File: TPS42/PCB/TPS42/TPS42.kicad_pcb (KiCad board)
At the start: 2 copper layers, 138.1 x 89.7 mm, 67 parts, among them J11 Conn_01x06, J3 TP Sensor Module, J4 TP Module, J5 Conn_01x02, J7 TrackPoint, J8 Battery, J9 TP Sensor Module, SW1 SW_DPST_x2, SW2 Reset, SW3 Reset, U1 ProMicro, U11 Hole, U12 Hole, U14 ProMicro, U4 Hole, U5 Hole, U7 Hole, U8 Hole, U9 Hole

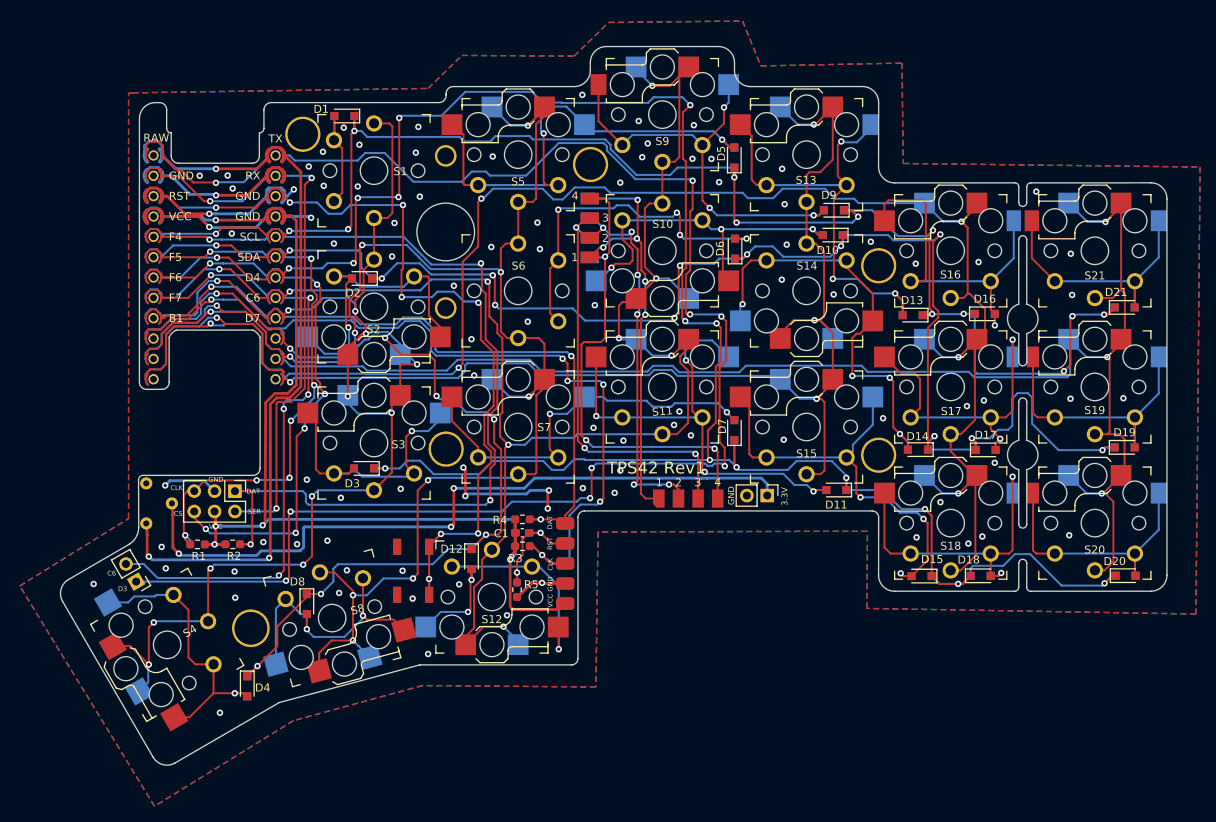
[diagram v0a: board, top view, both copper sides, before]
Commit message: TPS42: clean up the pcb a bit, get rid of the oled/lcd shields
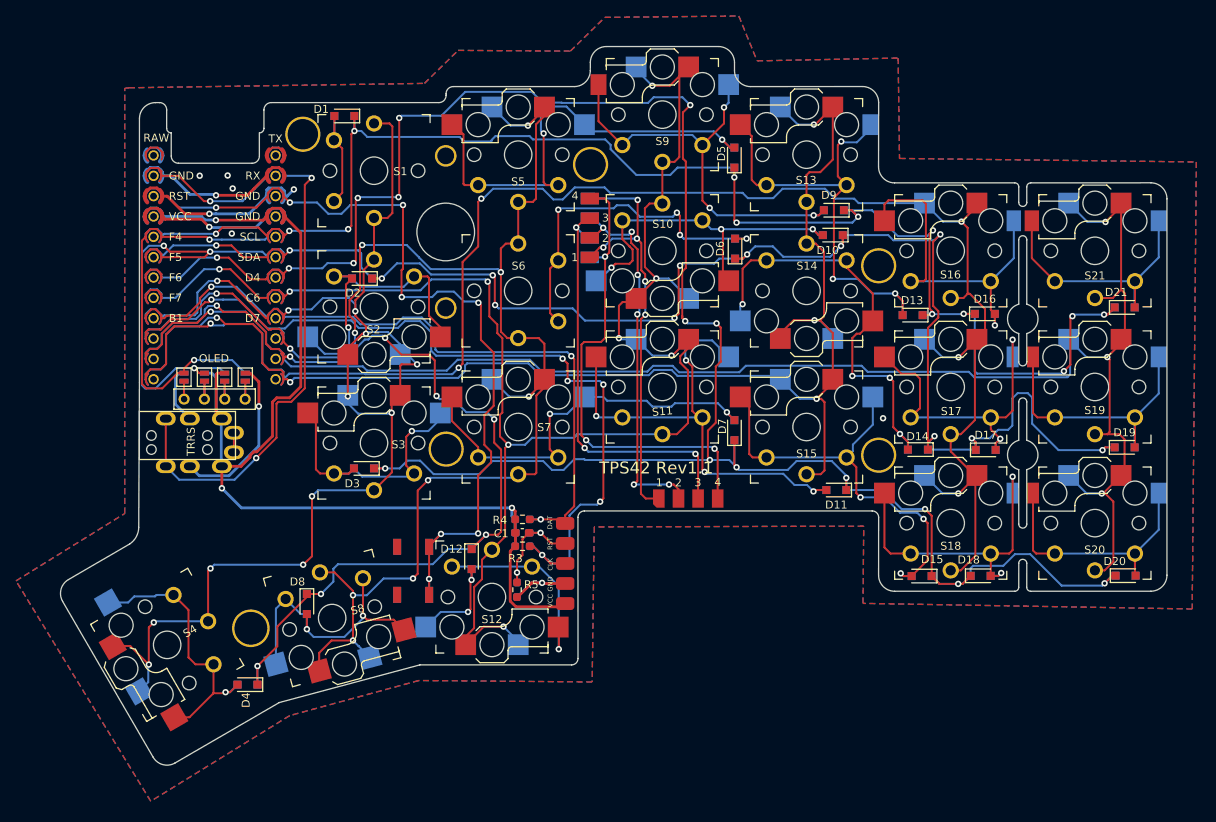
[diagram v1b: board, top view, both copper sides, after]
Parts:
- removed J11: Conn_01x06, Connector_PinHeader_2.54mm:PinHeader_2x03_P2.54mm_Vertical
- removed J5: Conn_01x02, Connector_PinHeader_2.54mm:PinHeader_1x02_P2.54mm_Vertical
- removed J8: Battery, Connector_PinHeader_2.54mm:PinHeader_1x02_P2.54mm_Vertical
- removed R1, R2: 4.7kΩ, TPS42:R_0603_1608Metric_Pad0.98x0.95mm_HandSolder_Reversable
- removed SW1: SW_DPST_x2, TPS42:SW-TH_3P-L9.1-W3.5-P2.50-S3.20-A3
- added J1: MJ-4PP-9, kbd:MJ-4PP-9, F.Cu at (83.0, 83.8)
- added J2: OLED, kbd:OLED, F.Cu at (88.6, 79.3)
- added JP1: , kbd:Jumper, F.Cu at (96.2, 76.5)
- added JP2: , kbd:Jumper, F.Cu at (93.6, 76.5)
- added JP3: , kbd:Jumper, F.Cu at (91.1, 76.5)
- added JP4: , kbd:Jumper, F.Cu at (88.5, 76.5)
- added JP5: , kbd:Jumper, B.Cu at (96.2, 76.5)
- added JP6: , kbd:Jumper, B.Cu at (93.6, 76.5)
- added JP7: , kbd:Jumper, B.Cu at (91.1, 76.5)
- added JP8: , kbd:Jumper, B.Cu at (88.6, 76.5)
- moved D4 0.20 mm to (96.5, 114.9), turned to 180 degrees
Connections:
- net CLK renamed SCL
- net DAT renamed SDA
- U1 pad 1: D3 -> unconnected-(U1-TX0/D3-Pad1)
- U1 pad 24: BAT+ -> unconnected-(U1-RAW-Pad24)
- U1 pad 7: CS -> unconnected-(U1-4/D4-Pad7)
- U1 pad 8: C6 -> unconnected-(U1-5/C6-Pad8)
- U14 pad 1: D3 -> unconnected-(U14-TX0/D3-Pad1)
- U14 pad 24: BAT+ -> unconnected-(U14-RAW-Pad24)
- U14 pad 7: CS -> unconnected-(U14-4/D4-Pad7)
- U14 pad 8: C6 -> unconnected-(U14-5/C6-Pad8)
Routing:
- net D3: track 210.1 -> 0.00 mm, vias 9 -> 0
- net BAT+: track 96.6 -> 0.00 mm, vias 3 -> 0
- net Net-(J8-Pad1): track 90.0 -> 0.00 mm, vias 3 -> 0
- net C6: track 83.0 -> 0.00 mm, vias 5 -> 0
- net CS: track 73.5 -> 0.00 mm, vias 6 -> 0
- net SDA: track 122.3 -> 54.2 mm, vias 4 -> 2
- net SCL: track 75.3 -> 59.5 mm, vias 7 -> 3
- net VCC: track 133.9 -> 143.6 mm, vias 5 -> 3
- net SERIAL: track 75.5 -> 84.0 mm
- net Net-(J2-Pin_4): track 0.00 -> 4.49 mm
- net Net-(J2-Pin_3): track 0.00 -> 4.48 mm
- net Net-(J2-Pin_2): track 0.00 -> 4.48 mm
- net Net-(J2-Pin_1): track 0.00 -> 4.48 mm
- net unconnected-(U14-TX0/D3-Pad1): track 0.00 -> 3.37 mm
- net unconnected-(U14-RAW-Pad24): track 0.00 -> 3.33 mm
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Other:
- outline, holes or cut-outs redrawn
- board text added: "TPS42 Rev1.1"
- board text removed: "3.3V"
- board text removed: "C6"
- board text removed: "CS"
- board text removed: "D3"
- board text removed: "SER"
- board text removed: "TPS42 Rev${Revision}"

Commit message: TPS42: bump version
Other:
- board text added: "TPS42 2b74dfa"
- board text removed: "TPS42 Rev1.1"
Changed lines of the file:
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@@
     (fp_line (start 7 7) (end 6 7)
       (stroke (width 0.15) (type solid)) (layer "F.SilkS"))
-    (fp_arc (start -2.5 -2.2) (mid -2.06066 -3.26066) (end -1 -3.7)
+    (fp_arc (start -2.5 -2.2) (mid -2.060659 -3.26066) (end -1 -3.7)
       (stroke (width 0.15) (type solid)) (layer "F.SilkS"))
     (fp_arc (start -2 -6.7) (mid -2.146447 -6.346447) (end -2.5 -6.2)
@@
     (fp_line (start 7.5 7.5) (end -7.5 7.5)
       (stroke (width 0.15) (type solid)) (layer "F.Fab"))
-    (fp_arc (start -2.5 -2.2) (mid -2.06066 -3.26066) (end -1 -3.7)
+    (fp_arc (start -2.5 -2.2) (mid -2.060659 -3.26066) (end -1 -3.7)
       (stroke (width 0.15) (type solid)) (layer "F.Fab"))
     (fp_arc (start -2 -6.7) (mid -2.146447 -6.346447) (end -2.5 -6.2)
@@
     (effects (font (size 1 1) (thickness 0.15)) (justify mirror))
   )
-  (gr_text "TPS42 Rev1.1" (at 147.33 87.83) (layer "B.SilkS")
+  (gr_text "TPS42 2b74dfa" (at 147.33 87.83) (layer "B.SilkS")
     (effects (font (size 1.5 1.5) (thickness 0.3)) (justify mirror))
   )
@@
     (effects (font (size 0.6 0.6) (thickness 0.1)))
   )
-  (gr_text "TPS42 Rev1.1" (at 147.51 87.86) (layer "F.SilkS")
+  (gr_text "TPS42 2b74dfa" (at 147.51 87.86) (layer "F.SilkS")
     (effects (font (size 1.5 1.5) (thickness 0.3)))
   )
